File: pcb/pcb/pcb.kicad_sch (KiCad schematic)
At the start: 28 parts, among them J1 Conn_01x28_Socket, J2 Conn_01x28_Socket, J3 Conn_01x03_Socket, J4 Conn_01x04_Socket, J5 MAX17048, J6 LSM6DS3TR-C, J7 SSD1306, SW1 SW_SPST, U1 TPS61022

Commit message: pcb layout, calorie model
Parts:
- C1, C2, C3, C4, C5, C6, C7, C8: footprint (none) -> Capacitor_SMD:C_0805_2012Metric_Pad1.18x1.45mm_HandSolder
- J1, J2: footprint (none) -> Connector_PinSocket_2.54mm:PinSocket_1x28_P2.54mm_Vertical
- J3: footprint (none) -> Connector_PinSocket_2.54mm:PinSocket_1x03_P2.54mm_Vertical
- J4, J7: footprint (none) -> Connector_PinSocket_2.54mm:PinSocket_1x04_P2.54mm_Vertical
- J5: footprint (none) -> Connector_PinSocket_2.54mm:PinSocket_1x06_P2.54mm_Vertical
- J6: footprint (none) -> Connector_PinSocket_2.54mm:PinSocket_1x09_P2.54mm_Vertical
- L1: footprint (none) -> Inductor_SMD:L_0805_2012Metric_Pad1.05x1.20mm_HandSolder
- NT1: footprint (none) -> NetTie:NetTie-2_SMD_Pad0.5mm
- R1, R2, R3, R4, R5: footprint (none) -> Resistor_SMD:R_0805_2012Metric_Pad1.20x1.40mm_HandSolder
- SW1: footprint (none) -> Button_Switch_SMD:SW_DIP_SPSTx01_Slide_6.7x4.1mm_W6.73mm_P2.54mm_LowProfile_JPin
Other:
- moved on the sheet: C1, C2, C3, C4
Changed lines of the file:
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@@
 	(wire
 		(pts
-			(xy 162.56 107.95) (xy 162.56 113.03)
+			(xy 162.56 109.22) (xy 162.56 113.03)
 		)
 		(stroke
@@
 	(wire
 		(pts
-			(xy 226.06 97.79) (xy 226.06 100.33)
+			(xy 226.06 97.79) (xy 226.06 101.6)
 		)
 		(stroke
@@
 	(wire
 		(pts
-			(xy 226.06 107.95) (xy 226.06 113.03)
+			(xy 226.06 109.22) (xy 226.06 113.03)
 		)
 		(stroke
@@
 	(wire
 		(pts
-			(xy 195.58 97.79) (xy 195.58 100.33)
+			(xy 195.58 97.79) (xy 195.58 101.6)
 		)
 		(stroke
@@
 	(wire
 		(pts
-			(xy 255.27 97.79) (xy 255.27 100.33)
+			(xy 255.27 97.79) (xy 255.27 101.6)
 		)
 		(stroke
@@
 	(wire
 		(pts
-			(xy 195.58 107.95) (xy 195.58 113.03)
+			(xy 195.58 109.22) (xy 195.58 113.03)
 		)
 		(stroke
@@
 	(wire
 		(pts
-			(xy 162.56 97.79) (xy 162.56 100.33)
+			(xy 162.56 97.79) (xy 162.56 101.6)
 		)
 		(stroke
@@
 	(wire
 		(pts
-			(xy 255.27 107.95) (xy 255.27 113.03)
+			(xy 255.27 109.22) (xy 255.27 113.03)
 		)
 		(stroke
@@
 			)
 		)
-		(property "Footprint" ""
+		(property "Footprint" "Connector_PinSocket_2.54mm:PinSocket_1x04_P2.54mm_Vertical"
 			(at 20.32 133.35 0)
 			(effects
@@
 			)
 		)
-		(property "Footprint" ""
+		(property "Footprint" "Button_Switch_SMD:SW_DIP_SPSTx01_Slide_6.7x4.1mm_W6.73mm_P2.54mm_LowProfile_JPin"
 			(at 186.69 52.07 0)
 			(effects
@@
 			)
 		)
-		(property "Footprint" ""
+		(property "Footprint" "Connector_PinSocket_2.54mm:PinSocket_1x04_P2.54mm_Vertical"
 			(at 127 179.07 0)
 			(effects
@@
 	(symbol
 		(lib_id "Device:C")
-		(at 255.27 104.14 0)
+		(at 255.27 105.41 0)
 		(unit 1)
 		(exclude_from_sim no)
@@
 		(fields_autoplaced yes)
 		(property "Reference" "C4"
-			(at 259.08 102.8699 0)
+			(at 259.08 104.1399 0)
 			(effects
 				(font
@@
 		)
 		(property "Value" "0.1uF"
-			(at 259.08 105.4099 0)
+			(at 259.08 106.6799 0)
 			(effects
 				(font
@@
 			)
 		)
-		(property "Footprint" ""
-			(at 256.2352 107.95 0)
+		(property "Footprint" "Capacitor_SMD:C_0805_2012Metric_Pad1.18x1.45mm_HandSolder"
+			(at 256.2352 109.22 0)
 			(effects
 				(font
@@
 		)
 		(property "Datasheet" "~"
-			(at 255.27 104.14 0)
+			(at 255.27 105.41 0)
 			(effects
 				(font
@@
 		)
 		(property "Description" "Unpolarized capacitor"
-			(at 255.27 104.14 0)
+			(at 255.27 105.41 0)
 			(effects
 				(font
@@
 	(symbol
 		(lib_id "Device:C")
-		(at 195.58 104.14 0)
+		(at 195.58 105.41 0)
 		(unit 1)
 		(exclude_from_sim no)
@@
 		(fields_autoplaced yes)
 		(property "Reference" "C2"
-			(at 199.39 102.8699 0)
+			(at 199.39 104.1399 0)
 			(effects
 				(font
@@
 		)
 		(property "Value" "0.1uF"
-			(at 199.39 105.4099 0)
+			(at 199.39 106.6799 0)
 			(effects
 				(font
@@
 			)
 		)
-		(property "Footprint" ""
-			(at 196.5452 107.95 0)
+		(property "Footprint" "Capacitor_SMD:C_0805_2012Metric_Pad1.18x1.45mm_HandSolder"
+			(at 196.5452 109.22 0)
 			(effects
 				(font
@@
 		)
 		(property "Datasheet" "~"
-			(at 195.58 104.14 0)
+			(at 195.58 105.41 0)
 			(effects
 				(font
@@
 		)
 		(property "Description" "Unpolarized capacitor"
-			(at 195.58 104.14 0)
+			(at 195.58 105.41 0)
 			(effects
 				(font
@@
 			)
 		)
-		(property "Footprint" ""
+		(property "Footprint" "Capacitor_SMD:C_0805_2012Metric_Pad1.18x1.45mm_HandSolder"
 			(at 257.81 52.07 0)
 			(effects
@@
 			)
 		)
-		(property "Footprint" ""
+		(property "Footprint" "Resistor_SMD:R_0805_2012Metric_Pad1.20x1.40mm_HandSolder"
 			(at 229.87 57.15 0)
 			(effects
@@
 	(symbol
 		(lib_id "Device:C")
-		(at 226.06 104.14 0)
+		(at 226.06 105.41 0)
 		(unit 1)
 		(exclude_from_sim no)
@@
 		(fields_autoplaced yes)
 		(property "Reference" "C3"
-			(at 229.87 102.8699 0)
+			(at 229.87 104.1399 0)
 			(effects
 				(font
@@
 		)
 		(property "Value" "0.1uF"
-			(at 229.87 105.4099 0)
+			(at 229.87 106.6799 0)
 			(effects
 				(font
@@
 			)
 		)
-		(property "Footprint" ""
-			(at 227.0252 107.95 0)
+		(property "Footprint" "Capacitor_SMD:C_0805_2012Metric_Pad1.18x1.45mm_HandSolder"
+			(at 227.0252 109.22 0)
 			(effects
 				(font
@@
 		)
 		(property "Datasheet" "~"
-			(at 226.06 104.14 0)
+			(at 226.06 105.41 0)
 			(effects
 				(font
@@
 		)
 		(property "Description" "Unpolarized capacitor"
-			(at 226.06 104.14 0)
+			(at 226.06 105.41 0)
 			(effects
 				(font
@@
 			)
 		)
-		(property "Footprint" ""
+		(property "Footprint" "Capacitor_SMD:C_0805_2012Metric_Pad1.18x1.45mm_HandSolder"
 			(at 194.31 38.1 0)
 			(effects
@@
 			)
 		)
-		(property "Footprint" ""
+		(property "Footprint" "Connector_PinSocket_2.54mm:PinSocket_1x28_P2.54mm_Vertical"
 			(at 127 120.65 0)
 			(effects
@@
 			)
 		)
-		(property "Footprint" ""
+		(property "Footprint" "Capacitor_SMD:C_0805_2012Metric_Pad1.18x1.45mm_HandSolder"
 			(at 265.43 52.07 0)
 			(effects
@@
 			)
 		)
-		(property "Footprint" ""
+		(property "Footprint" "Resistor_SMD:R_0805_2012Metric_Pad1.20x1.40mm_HandSolder"
 			(at 229.87 52.07 0)
 			(effects
@@
 			)
 		)
-		(property "Footprint" ""
+		(property "Footprint" "Connector_PinSocket_2.54mm:PinSocket_1x03_P2.54mm_Vertical"
 			(at 62.23 179.07 0)
 			(effects
@@
 			)
 		)
-		(property "Footprint" ""
+		(property "Footprint" "Resistor_SMD:R_0805_2012Metric_Pad1.20x1.40mm_HandSolder"
 			(at 237.49 52.07 0)
 			(effects
@@
 			)
 		)
-		(property "Footprint" ""
+		(property "Footprint" "Connector_PinSocket_2.54mm:PinSocket_1x06_P2.54mm_Vertical"
 			(at 20.32 156.21 0)
 			(effects
@@
 			)
 		)
-		(property "Footprint" ""
+		(property "Footprint" "Connector_PinSocket_2.54mm:PinSocket_1x28_P2.54mm_Vertical"
 			(at 62.23 120.65 0)
 			(effects
@@
 	(symbol
 		(lib_id "Device:C")
-		(at 162.56 104.14 0)
+		(at 162.56 105.41 0)
 		(unit 1)
 		(exclude_from_sim no)
@@
 		(fields_autoplaced yes)
 		(property "Reference" "C1"
-			(at 166.37 102.8699 0)
+			(at 166.37 104.1399 0)
 			(effects
 				(font
@@
 		)
 		(property "Value" "500u"
-			(at 166.37 105.4099 0)
+			(at 166.37 106.6799 0)
 			(effects
 				(font
@@
 			)
 		)
-		(property "Footprint" ""
-			(at 163.5252 107.95 0)
+		(property "Footprint" "Capacitor_SMD:C_0805_2012Metric_Pad1.18x1.45mm_HandSolder"
+			(at 163.5252 109.22 0)
 			(effects
 				(font
@@
 		)
 		(property "Datasheet" "~"
-			(at 162.56 104.14 0)
+			(at 162.56 105.41 0)
 			(effects
 				(font
@@
 		)
 		(property "Description" "Unpolarized capacitor"
-			(at 162.56 104.14 0)
+			(at 162.56 105.41 0)
 			(effects
 				(font
@@
 			)
 		)
-		(property "Footprint" ""
+		(property "Footprint" "Resistor_SMD:R_0805_2012Metric_Pad1.20x1.40mm_HandSolder"
 			(at 194.31 58.42 0)
 			(effects
@@
 			)
 		)
-		(property "Footprint" ""
+		(property "Footprint" "Resistor_SMD:R_0805_2012Metric_Pad1.20x1.40mm_HandSolder"
 			(at 171.704 120.396 90)
 			(effects
@@
 			)
 		)
-		(property "Footprint" ""
+		(property "Footprint" "Connector_PinSocket_2.54mm:PinSocket_1x09_P2.54mm_Vertical"
 			(at 20.32 182.88 0)
 			(effects
@@
 			)
 		)
-		(property "Footprint" ""
+		(property "Footprint" "Inductor_SMD:L_0805_2012Metric_Pad1.05x1.20mm_HandSolder"
 			(at 210.82 35.56 0)
 			(effects
@@
 			)
 		)
-		(property "Footprint" ""
+		(property "Footprint" "NetTie:NetTie-2_SMD_Pad0.5mm"
 			(at 116.84 73.66 0)
 			(effects
@@
 			)
 		)
-		(property "Footprint" ""
+		(property "Footprint" "Capacitor_SMD:C_0805_2012Metric_Pad1.18x1.45mm_HandSolder"
 			(at 250.19 52.07 0)
 			(effects

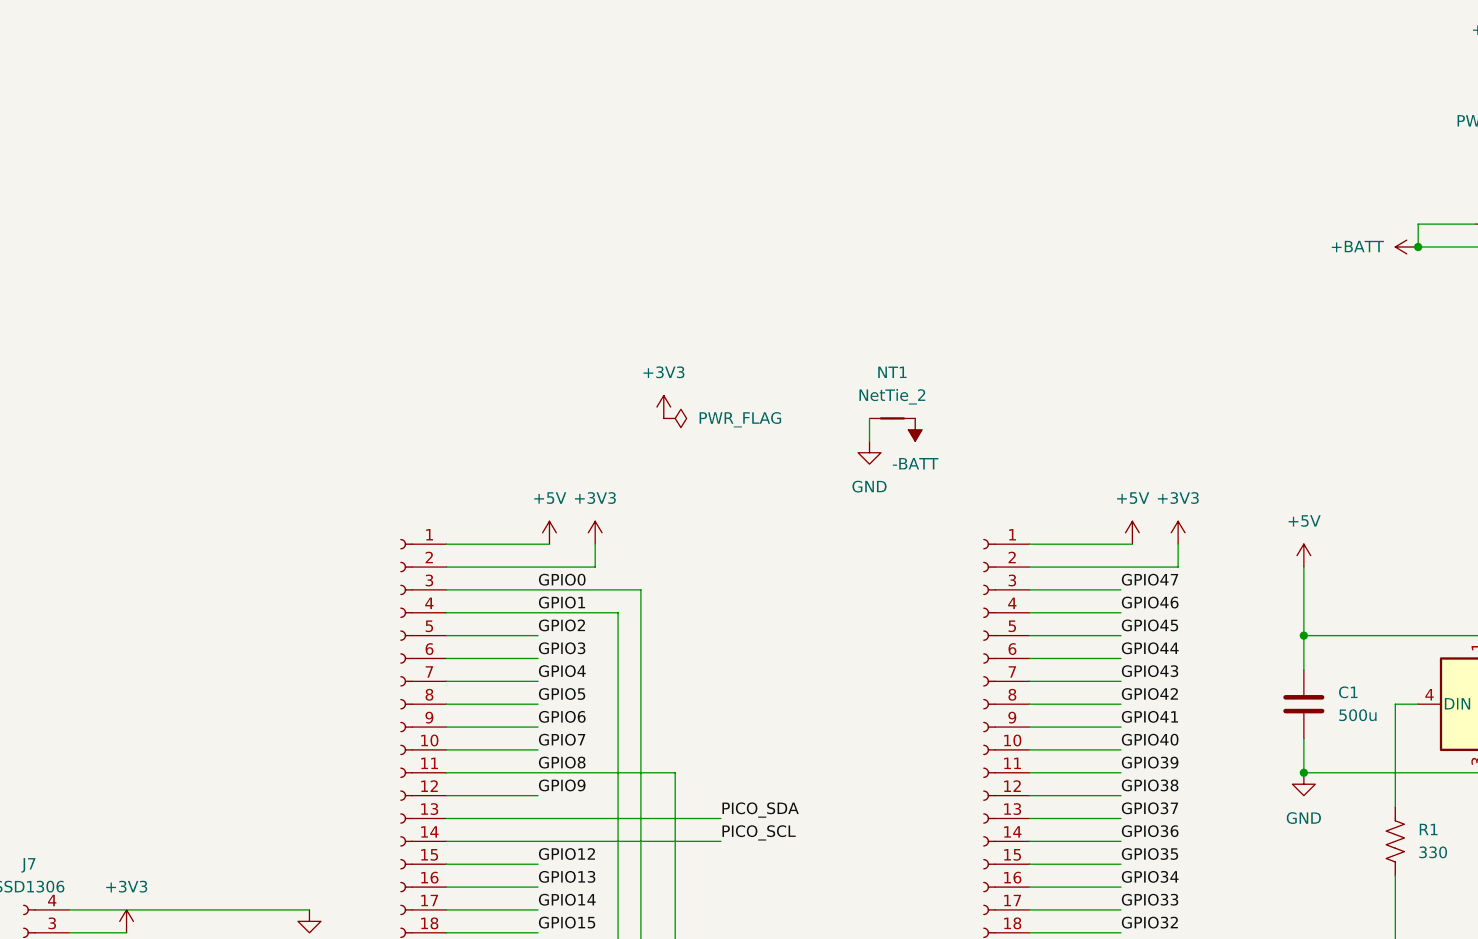
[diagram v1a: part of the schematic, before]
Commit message: add test points 2
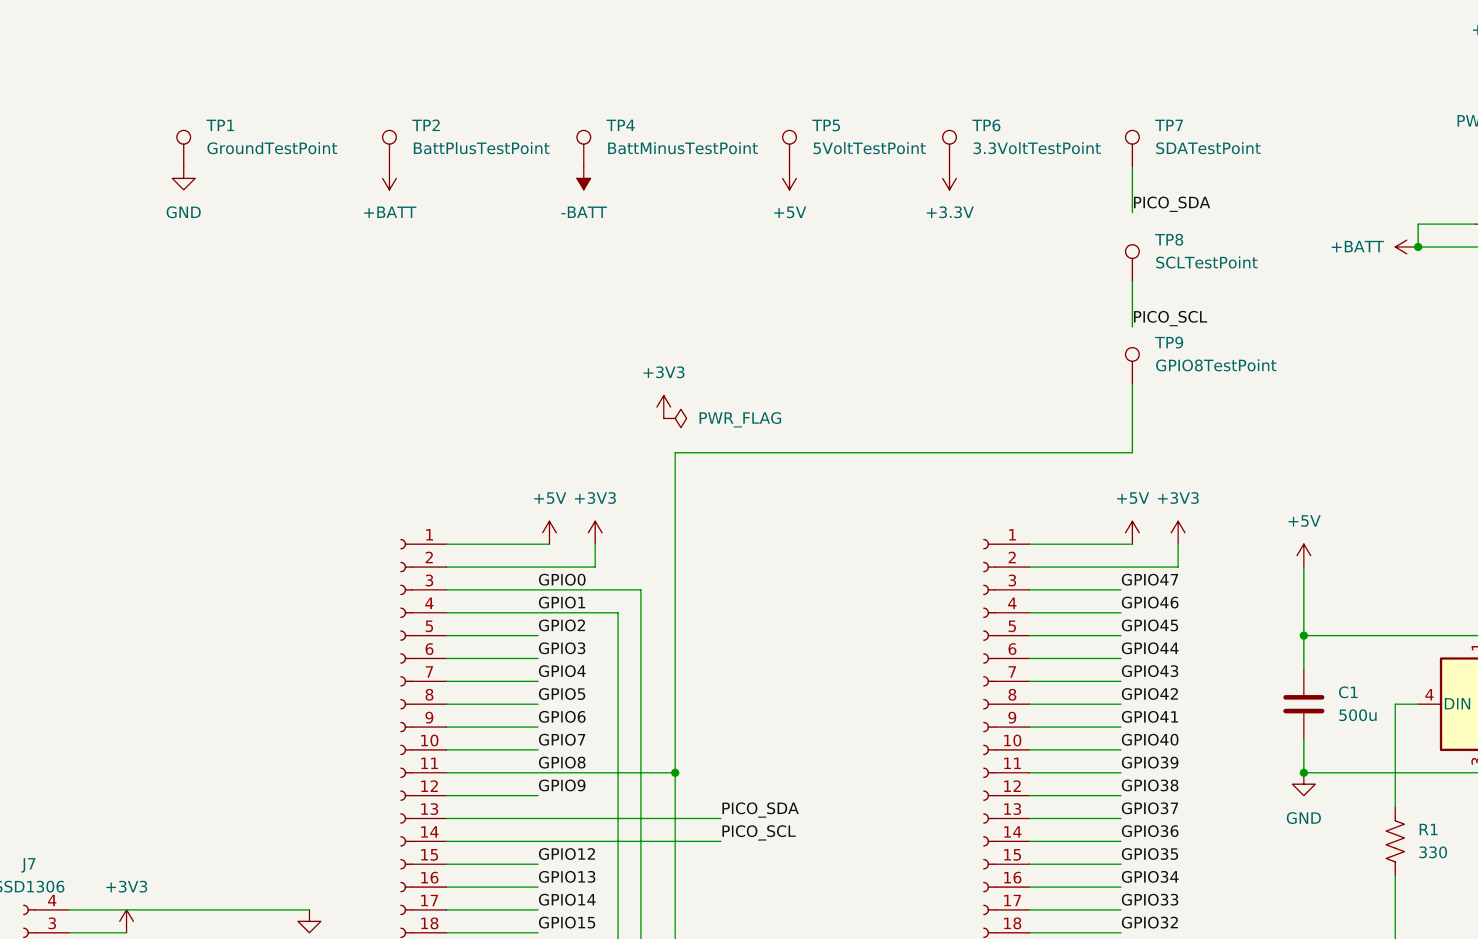
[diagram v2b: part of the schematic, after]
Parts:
- removed NT1: NetTie_2, NetTie:NetTie-2_SMD_Pad0.5mm, symbol Device:NetTie_2
- added TP1: GroundTestPoint, symbol Connector:TestPoint
- added TP2: BattPlusTestPoint, symbol Connector:TestPoint
- added TP4: BattMinusTestPoint, symbol Connector:TestPoint
- added TP5: 5VoltTestPoint, symbol Connector:TestPoint
- added TP6: 3.3VoltTestPoint, symbol Connector:TestPoint
- added TP7: SDATestPoint, symbol Connector:TestPoint
- added TP8: SCLTestPoint, symbol Connector:TestPoint
- added TP9: GPIO8TestPoint, symbol Connector:TestPoint
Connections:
- net +5V: now also TP5.1
- net +BATT: now also TP2.1
- net -BATT: now also TP4.1
- net GND: now also TP1.1
- net GPIO8: now also TP9.1
- net PICO_SCL: now also TP8.1
- net PICO_SDA: now also TP7.1
- new net +3.3V: TP6.1

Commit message: finished pcb
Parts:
- TP1, TP2, TP4, TP5, TP6, TP7, TP8, TP9: footprint (none) -> TestPoint:TestPoint_Pad_D1.5mm
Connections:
- net GND is gone; now on net -BATT: C1.2, C2.2, C3.2, C4.2, C5.2, C6.2, C7.2, C8.2, D1.3 (VSS), D2.3 (VSS), D3.3 (VSS), D4.3 (VSS), J1.28 (Pin_28), J2.28 (Pin_28), J3.2 (Pin_2), J4.3 (Pin_3), J5.5 (Pin_5), J6.7 (Pin_7), J7.4 (Pin_4), R3.2, R5.2, TP1.1, U1.1 (GND)
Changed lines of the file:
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@@
 			)
 		)
-		(property "Footprint" ""
+		(property "Footprint" "TestPoint:TestPoint_Pad_D1.5mm"
 			(at 148.59 58.42 0)
 			(effects
@@
 	)
 	(symbol
+		(lib_id "power:-BATT")
+		(at 60.96 62.23 0)
+		(unit 1)
+		(exclude_from_sim no)
+		(in_bom yes)
+		(on_board yes)
+		(dnp no)
+		(fields_autoplaced yes)
+		(property "Reference" "#PWR030"
+			(at 60.96 66.04 0)
+			(effects
+				(font
+					(size 1.27 1.27)
+				)
+				(hide yes)
+			)
+		)
+		(property "Value" "-BATT"
+			(at 60.96 57.15 0)
+			(effects
+				(font
+					(size 1.27 1.27)
+				)
+			)
+		)
+		(property "Footprint" ""
+			(at 60.96 62.23 0)
+			(effects
+				(font
+					(size 1.27 1.27)
+				)
+				(hide yes)
+			)
+		)
+		(property "Datasheet" ""
+			(at 60.96 62.23 0)
+			(effects
+				(font
+					(size 1.27 1.27)
+				)
+				(hide yes)
+			)
+		)
+		(property "Description" "Power symbol creates a global label with name \"-BATT\""
+			(at 60.96 62.23 0)
+			(effects
+				(font
+					(size 1.27 1.27)
+				)
+				(hide yes)
+			)
+		)
+		(pin "1"
+		)
+		(instances
+			(project ""
+				(path "/ed8a14d0-1436-4c55-bdca-bec03d616b0a"
+					(reference "#PWR030")
+					(unit 1)
+				)
+			)
+		)
+	)
+	(symbol
 		(lib_id "power:+3V3")
 		(at 91.44 73.66 0)
@@
 			)
 		)
-		(property "Footprint" ""
+		(property "Footprint" "TestPoint:TestPoint_Pad_D1.5mm"
 			(at 87.63 45.72 0)
 			(effects
@@
 			)
 		)
-		(property "Footprint" ""
+		(property "Footprint" "TestPoint:TestPoint_Pad_D1.5mm"
 			(at 43.18 45.72 0)
 			(effects
@@
 			)
 		)
-		(property "Footprint" ""
+		(property "Footprint" "TestPoint:TestPoint_Pad_D1.5mm"
 			(at 148.59 69.85 0)
 			(effects
@@
 			)
 		)
-		(property "Footprint" ""
+		(property "Footprint" "TestPoint:TestPoint_Pad_D1.5mm"
 			(at 128.27 45.72 0)
 			(effects
@@
 	)
 	(symbol
+		(lib_id "power:GND")
+		(at 60.96 62.23 0)
+		(unit 1)
+		(exclude_from_sim no)
+		(in_bom yes)
+		(on_board yes)
+		(dnp no)
+		(fields_autoplaced yes)
+		(property "Reference" "#PWR032"
+			(at 60.96 68.58 0)
+			(effects
+				(font
+					(size 1.27 1.27)
+				)
+				(hide yes)
+			)
+		)
+		(property "Value" "GND"
+			(at 60.96 67.31 0)
+			(effects
+				(font
+					(size 1.27 1.27)
+				)
+			)
+		)
+		(property "Footprint" ""
+			(at 60.96 62.23 0)
+			(effects
+				(font
+					(size 1.27 1.27)
+				)
+				(hide yes)
+			)
+		)
+		(property "Datasheet" ""
+			(at 60.96 62.23 0)
+			(effects
+				(font
+					(size 1.27 1.27)
+				)
+				(hide yes)
+			)
+		)
+		(property "Description" "Power symbol creates a global label with name \"GND\" , ground"
+			(at 60.96 62.23 0)
+			(effects
+				(font
+					(size 1.27 1.27)
+				)
+				(hide yes)
+			)
+		)
+		(pin "1"
+		)
+		(instances
+			(project ""
+				(path "/ed8a14d0-1436-4c55-bdca-bec03d616b0a"
+					(reference "#PWR032")
+					(unit 1)
+				)
+			)
+		)
+	)
+	(symbol
 		(lib_id "power:+5V")
 		(at 105.41 45.72 180)
@@
 			)
 		)
-		(property "Footprint" ""
+		(property "Footprint" "TestPoint:TestPoint_Pad_D1.5mm"
 			(at 110.49 45.72 0)
 			(effects
@@
 			)
 		)
-		(property "Footprint" ""
+		(property "Footprint" "TestPoint:TestPoint_Pad_D1.5mm"
 			(at 66.04 45.72 0)
 			(effects
@@
 			)
 		)
-		(property "Footprint" ""
+		(property "Footprint" "TestPoint:TestPoint_Pad_D1.5mm"
 			(at 148.59 45.72 0)
 			(effects
